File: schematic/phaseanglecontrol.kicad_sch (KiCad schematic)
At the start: 35 parts, among them J1 L_supply, J2 N_supply, J3 motor_housing, J4 N_motor, J5 L_motor, Q1 IRFP450, Q2 BS170, Q3 IRFR9310, Q4 IRFP450, U1 ATtiny861A-P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

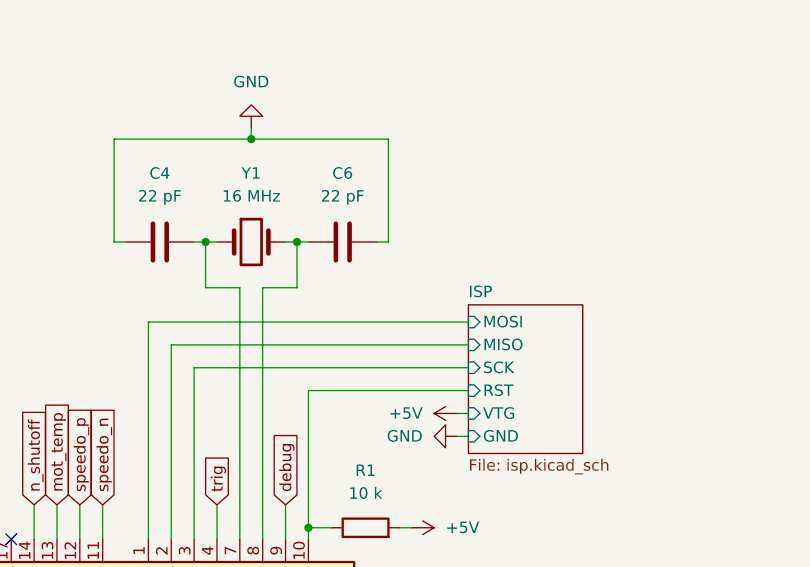
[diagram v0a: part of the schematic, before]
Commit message: schematic: Add uart tx
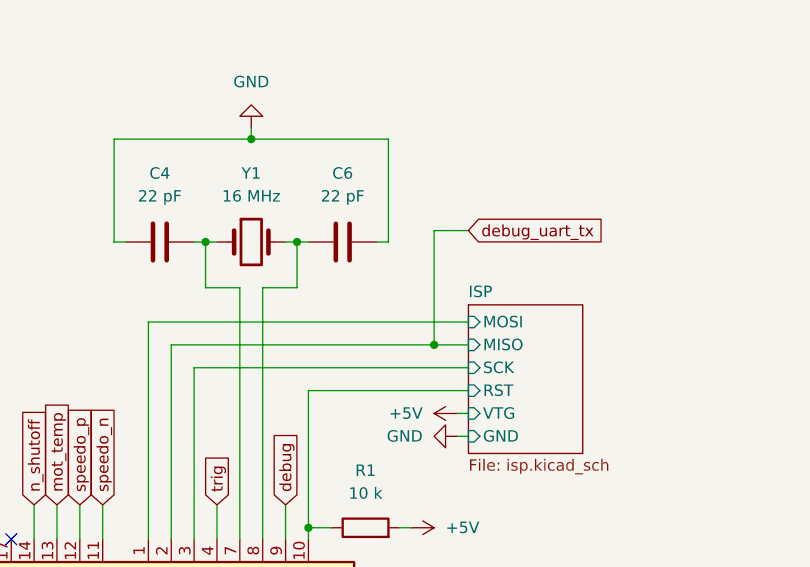
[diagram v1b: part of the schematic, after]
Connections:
- net ISP/MISO renamed debug_uart_tx
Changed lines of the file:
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@@
+	)
+	(junction
+		(at 105.41 128.27)
+		(diameter 0)
+		(color 0 0 0 0)
 	)
 	(junction
@@
 	(wire
 		(pts
-			(xy 76.2 128.27) (xy 109.22 128.27)
+			(xy 76.2 128.27) (xy 105.41 128.27)
 		)
 		(stroke
@@
 	(wire
 		(pts
+			(xy 105.41 115.57) (xy 105.41 128.27)
+		)
+		(stroke
+			(width 0)
+			(type default)
+		)
+	)
+	(wire
+		(pts
 			(xy 247.65 116.84) (xy 251.46 116.84)
 		)
@@
 	(wire
 		(pts
+			(xy 109.22 115.57) (xy 105.41 115.57)
+		)
+		(stroke
+			(width 0)
+			(type default)
+		)
+	)
+	(wire
+		(pts
 			(xy 172.72 111.76) (xy 168.91 111.76)
 		)
@@
 		(pts
 			(xy 137.16 27.94) (xy 147.32 27.94)
+		)
+		(stroke
+			(width 0)
+			(type default)
+		)
+	)
+	(wire
+		(pts
+			(xy 105.41 128.27) (xy 109.22 128.27)
 		)
 		(stroke
@@
 				(hide yes)
 			)
+		)
+	)
+	(global_label "debug_uart_tx"
+		(shape input)
+		(at 109.22 115.57 0)
+		(fields_autoplaced yes)
+		(effects
+			(font
+				(size 1.27 1.27)
+			)
+			(justify left)
+		)
+		(property "Intersheetrefs" "${INTERSHEET_REFS}"
+			(at 125.3887 115.57 0)
+			(effects
+				(font
+					(size 1.27 1.27)
+				)
+				(justify left)
+				(hide yes)
+			)

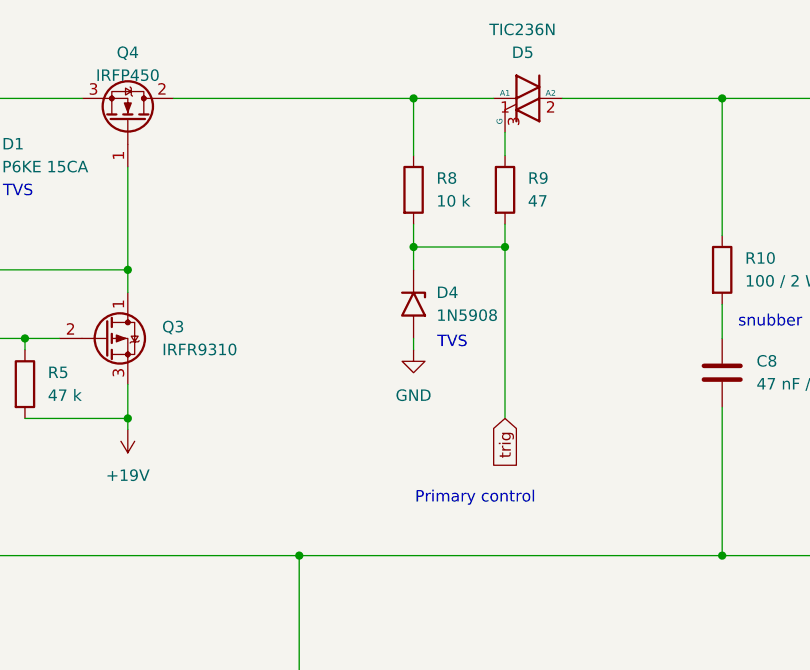
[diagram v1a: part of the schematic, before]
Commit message: schematic: Update trig resistor
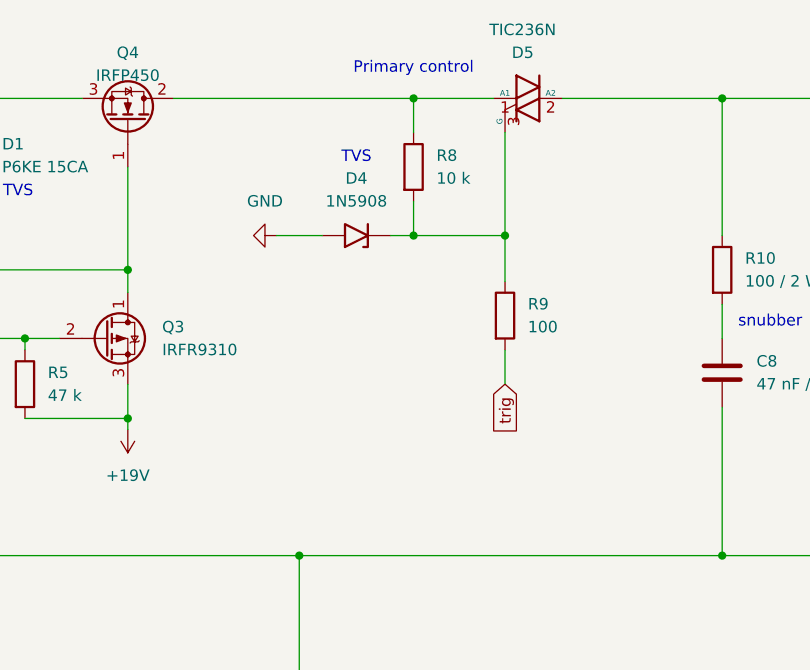
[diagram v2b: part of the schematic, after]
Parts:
- R9: value 47 -> 100
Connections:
- net trig: no longer D4.1 (A1), R8.2
- net at D5.3 (G), R9.1: now also D4.1 (A1), R8.2
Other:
- moved on the sheet: D4, R8, R9
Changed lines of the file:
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@@
 	(text "TVS"
 		(exclude_from_sim no)
-		(at 210.058 55.118 0)
+		(at 199.39 34.544 0)
 		(effects
 			(font
@@
 	(text "Primary control"
 		(exclude_from_sim no)
-		(at 212.598 72.39 0)
+		(at 205.74 24.638 0)
 		(effects
 			(font
@@
 	)
 	(junction
-		(at 60.96 27.94)
+		(at 205.74 43.18)
 		(diameter 0)
 		(color 0 0 0 0)
 	)
 	(junction
-		(at 137.16 27.94)
+		(at 60.96 27.94)
 		(diameter 0)
 		(color 0 0 0 0)
 	)
 	(junction
-		(at 147.32 27.94)
+		(at 137.16 27.94)
 		(diameter 0)
 		(color 0 0 0 0)
 	)
 	(junction
-		(at 157.48 46.99)
+		(at 147.32 27.94)
 		(diameter 0)
 		(color 0 0 0 0)
 	)
 	(junction
-		(at 205.74 44.45)
+		(at 157.48 46.99)
 		(diameter 0)
 		(color 0 0 0 0)
@@
 	)
 	(junction
-		(at 215.9 44.45)
+		(at 215.9 43.18)
 		(diameter 0)
 		(color 0 0 0 0)
@@
 	(wire
 		(pts
+			(xy 215.9 31.75) (xy 215.9 43.18)
+		)
+		(stroke
+			(width 0)
+			(type default)
+		)
+	)
+	(wire
+		(pts
 			(xy 193.04 78.74) (xy 240.03 78.74)
 		)
@@
 	(wire
 		(pts
-			(xy 215.9 31.75) (xy 215.9 34.29)
-		)
-		(stroke
-			(width 0)
-			(type default)
-		)
-	)
-	(wire
-		(pts
 			(xy 76.2 149.86) (xy 76.2 128.27)
 		)
@@
 	(wire
 		(pts
-			(xy 205.74 54.61) (xy 205.74 55.88)
-		)
-		(stroke
-			(width 0)
-			(type default)
-		)
-	)
-	(wire
-		(pts
 			(xy 222.25 27.94) (xy 240.03 27.94)
 		)
@@
 	(wire
 		(pts
-			(xy 205.74 41.91) (xy 205.74 44.45)
+			(xy 205.74 39.37) (xy 205.74 43.18)
 		)
 		(stroke
@@
 	(wire
 		(pts
+			(xy 190.5 43.18) (xy 195.58 43.18)
+		)
+		(stroke
+			(width 0)
+			(type default)
+		)
+	)
+	(wire
+		(pts
 			(xy 40.64 167.64) (xy 41.91 167.64)
 		)
@@
 	(wire
 		(pts
-			(xy 205.74 44.45) (xy 215.9 44.45)
+			(xy 205.74 43.18) (xy 215.9 43.18)
 		)
 		(stroke
@@
 	(wire
 		(pts
-			(xy 215.9 41.91) (xy 215.9 44.45)
-		)
-		(stroke
-			(width 0)
-			(type default)
-		)
-	)
-	(wire
-		(pts
 			(xy 137.16 46.99) (xy 147.32 46.99)
 		)
@@
 	(wire
 		(pts
-			(xy 205.74 44.45) (xy 205.74 46.99)
+			(xy 29.21 78.74) (xy 60.96 78.74)
 		)
 		(stroke
@@
 	(wire
 		(pts
-			(xy 29.21 78.74) (xy 60.96 78.74)
+			(xy 31.75 162.56) (xy 41.91 162.56)
 		)
 		(stroke
@@
 	(wire
 		(pts
-			(xy 31.75 162.56) (xy 41.91 162.56)
+			(xy 78.74 116.84) (xy 80.01 116.84)
 		)
 		(stroke
@@
 	(wire
 		(pts
-			(xy 78.74 116.84) (xy 80.01 116.84)
+			(xy 29.21 27.94) (xy 35.56 27.94)
 		)
 		(stroke
@@
 	(wire
 		(pts
-			(xy 29.21 27.94) (xy 35.56 27.94)
+			(xy 203.2 43.18) (xy 205.74 43.18)
 		)
 		(stroke
@@
 	(wire
 		(pts
-			(xy 205.74 27.94) (xy 205.74 34.29)
+			(xy 205.74 27.94) (xy 205.74 31.75)
 		)
 		(stroke
@@
 	(wire
 		(pts
-			(xy 215.9 44.45) (xy 215.9 63.5)
+			(xy 215.9 43.18) (xy 215.9 48.26)
 		)
 		(stroke
@@
 	(wire
 		(pts
+			(xy 215.9 55.88) (xy 215.9 59.69)
+		)
+		(stroke
+			(width 0)
+			(type default)
+		)
+	)
+	(wire
+		(pts
 			(xy 86.36 121.92) (xy 86.36 149.86)
 		)
@@
 	(global_label "trig"
 		(shape input)
-		(at 215.9 63.5 270)
+		(at 215.9 59.69 270)
 		(fields_autoplaced yes)
 		(effects
@@
 		)
 		(property "Intersheetrefs" "${INTERSHEET_REFS}"
-			(at 215.9 69.7509 90)
+			(at 215.9 65.9409 90)
 			(effects
 				(font
@@
 	(symbol
 		(lib_id "Diode:1N5908")
-		(at 205.74 50.8 270)
+		(at 199.39 43.18 180)
 		(unit 1)
 		(exclude_from_sim no)
@@
 		(fields_autoplaced yes)
 		(property "Reference" "D4"
-			(at 208.28 49.5299 90)
+			(at 199.39 36.83 0)
 			(effects
 				(font
 					(size 1.27 1.27)
 				)
-				(justify left)
 			)
 		)
 		(property "Value" "1N5908"
-			(at 208.28 52.0699 90)
+			(at 199.39 39.37 0)
 			(effects
 				(font
 					(size 1.27 1.27)
 				)
-				(justify left)
 			)
 		)
 		(property "Footprint" "Diode_THT:D_DO-201AE_P15.24mm_Horizontal"
-			(at 197.104 50.8 0)
+			(at 199.39 34.544 0)
 			(effects
 				(font
@@
 		)
 		(property "Datasheet" "https://www.st.com/resource/en/datasheet/1n5908.pdf"
-			(at 201.168 49.784 0)
+			(at 200.406 38.608 0)
 			(effects
 				(font
@@
 		)
 		(property "Description" "1500W (10/1000 μs) Unidirectional TVS Diode, VRM = 5V (IRM = 300 μA at 25°C), VBR = 6V, DO-201AE"
-			(at 199.136 50.8 0)
+			(at 199.39 36.576 0)
 			(effects
 				(font
@@
 	(symbol
 		(lib_id "Device:R")
-		(at 215.9 38.1 0)
+		(at 215.9 52.07 0)
 		(unit 1)
 		(exclude_from_sim no)
@@
 		(fields_autoplaced yes)
 		(property "Reference" "R9"
-			(at 218.44 36.8299 0)
+			(at 218.44 50.7999 0)
 			(effects
 				(font
@@
 			)
 		)
-		(property "Value" "47"
-			(at 218.44 39.3699 0)
+		(property "Value" "100"
+			(at 218.44 53.3399 0)
 			(effects
 				(font
@@
 		)
 		(property "Footprint" ""
-			(at 214.122 38.1 90)
+			(at 214.122 52.07 90)
 			(effects
 				(font
@@
 		)
 		(property "Datasheet" "~"
-			(at 215.9 38.1 0)
+			(at 215.9 52.07 0)
 			(effects
 				(font
@@
 		)
 		(property "Description" "Resistor"
-			(at 215.9 38.1 0)
+			(at 215.9 52.07 0)
 			(effects
 				(font
@@
 	(symbol
 		(lib_id "Device:R")
-		(at 205.74 38.1 0)
+		(at 205.74 35.56 0)
 		(unit 1)
 		(exclude_from_sim no)
@@
 		(fields_autoplaced yes)
 		(property "Reference" "R8"
-			(at 208.28 36.8299 0)
+			(at 208.28 34.2899 0)
 			(effects
 				(font
@@
 		)
 		(property "Value" "10 k"
-			(at 208.28 39.3699 0)
+			(at 208.28 36.8299 0)
 			(effects
 				(font
@@
 		)
 		(property "Footprint" ""
-			(at 203.962 38.1 90)
+			(at 203.962 35.56 90)
 			(effects
 				(font
@@
 		)
 		(property "Datasheet" "~"
-			(at 205.74 38.1 0)
+			(at 205.74 35.56 0)
 			(effects
 				(font
@@
 		)
 		(property "Description" "Resistor"
-			(at 205.74 38.1 0)
+			(at 205.74 35.56 0)
 			(effects
 				(font
@@
 	(symbol
 		(lib_id "power:GND")
-		(at 205.74 55.88 0)
+		(at 190.5 43.18 270)
 		(unit 1)
 		(exclude_from_sim no)
@@
 		(fields_autoplaced yes)
 		(property "Reference" "#PWR014"
-			(at 205.74 62.23 0)
+			(at 184.15 43.18 0)
 			(effects
 				(font
@@
 		)
 		(property "Value" "GND"
-			(at 205.74 60.96 0)
+			(at 189.23 39.37 90)
 			(effects
 				(font
@@
 		)
 		(property "Footprint" ""
-			(at 205.74 55.88 0)
+			(at 190.5 43.18 0)
 			(effects
 				(font
@@
 		)
 		(property "Datasheet" ""
-			(at 205.74 55.88 0)
+			(at 190.5 43.18 0)
 			(effects
 				(font
@@
 		)
 		(property "Description" "Power symbol creates a global label with name \"GND\" , ground"
-			(at 205.74 55.88 0)
+			(at 190.5 43.18 0)
 			(effects
 				(font

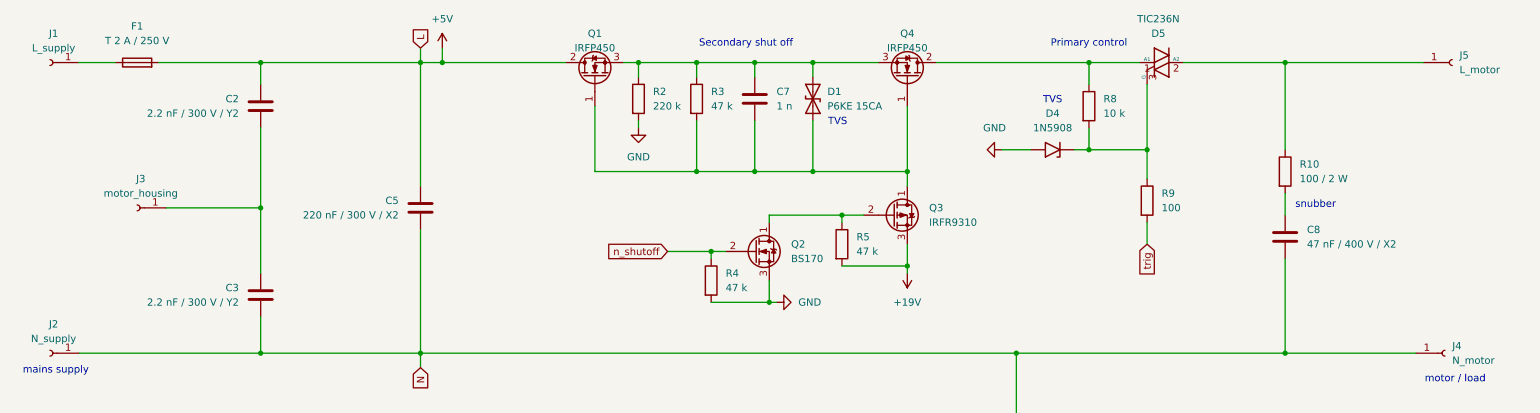
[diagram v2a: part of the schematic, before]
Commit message: schematic: Minor cleanups
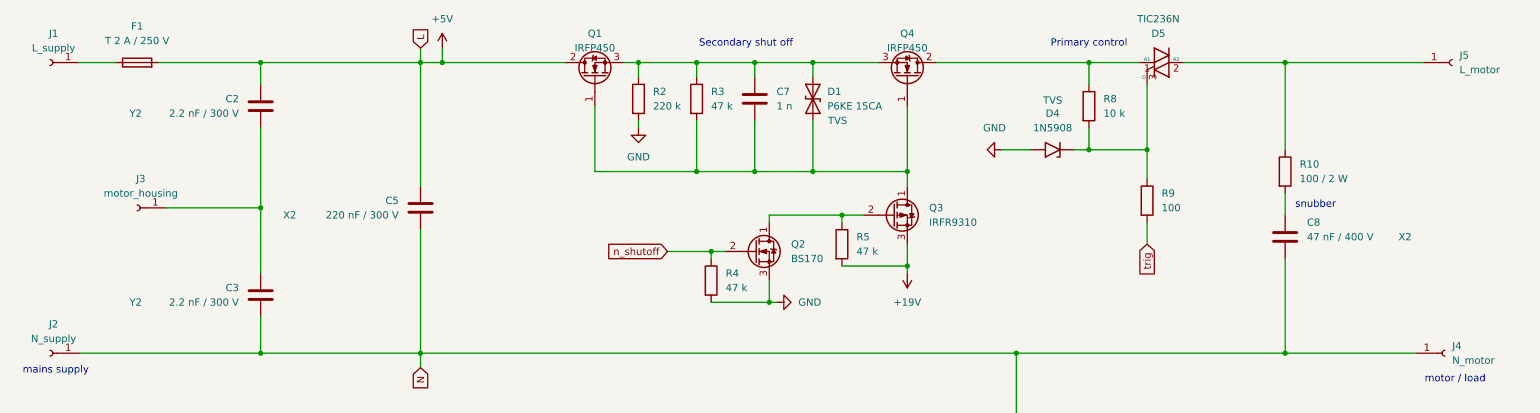
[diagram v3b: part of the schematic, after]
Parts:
- C2, C3: value 2.2 nF / 300 V / Y2 -> 2.2 nF / 300 V
- C5: value 220 nF / 300 V / X2 -> 220 nF / 300 V
- C8: value 47 nF / 400 V / X2 -> 47 nF / 400 V
- Q1, Q4: footprint Package_TO_SOT_THT:TO-247-3_Vertical -> (none)
- Q3: footprint Package_TO_SOT_THT:TO-92_Inline -> (none)
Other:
- note removed: "TVS"
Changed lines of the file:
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@@
 		(company "Michael Büsch <m@bues.ch>")
 	)
-	(text "TVS"
-		(exclude_from_sim no)
-		(at 199.39 34.544 0)
-		(effects
-			(font
-				(size 1.27 1.27)
-			)
-		)
-	)
 	(text "snubber"
 		(exclude_from_sim no)
@@
 		)
 	)
-	(text "TVS"
-		(exclude_from_sim no)
-		(at 161.798 38.354 0)
-		(effects
-			(font
-				(size 1.27 1.27)
-			)
-		)
-	)
 	(text "Primary control"
 		(exclude_from_sim no)
@@
 			)
 		)
-		(property "Value" "2.2 nF / 300 V / Y2"
+		(property "Value" "2.2 nF / 300 V"
 			(at 57.15 36.8299 0)
 			(effects
@@
 			)
 		)
-		(property "Description" "Unpolarized capacitor"
-			(at 60.96 35.56 0)
+		(property "Description" "Y2"
+			(at 39.116 36.83 0)
 			(effects
 				(font
 					(size 1.27 1.27)
 				)
-				(hide yes)
 			)
 		)
@@
 			)
 		)
-		(property "Footprint" "Package_TO_SOT_THT:TO-247-3_Vertical"
+		(property "Footprint" ""
 			(at 121.285 25.4 0)
 			(effects
@@
 			)
 		)
-		(property "Datasheet" "https://www.infineon.com/dgdl/irfp4468pbf.pdf?fileId=5546d462533600a40153562c73472019"
+		(property "Datasheet" ""
 			(at 123.19 25.4 0)
 			(effects
@@
 			)
 		)
-		(property "Description" "195A Id, 100V Vds, N-Channel Power MOSFET, TO-247"
+		(property "Description" ""
 			(at 119.38 30.48 0)
 			(effects
@@
 		(on_board yes)
 		(dnp no)
-		(fields_autoplaced yes)
 		(property "Reference" "D4"
 			(at 199.39 36.83 0)
@@
 			)
 		)
-		(property "Description" "1500W (10/1000 μs) Unidirectional TVS Diode, VRM = 5V (IRM = 300 μA at 25°C), VBR = 6V, DO-201AE"
-			(at 199.39 36.576 0)
+		(property "Description" "TVS"
+			(at 199.39 34.544 0)
 			(effects
 				(font
 					(size 1.27 1.27)
 				)
-				(hide yes)
 			)
 		)
@@
 			)
 		)
-		(property "Value" "2.2 nF / 300 V / Y2"
+		(property "Value" "2.2 nF / 300 V"
 			(at 57.15 69.8499 0)
 			(effects
@@
 			)
 		)
-		(property "Description" "Unpolarized capacitor"
-			(at 60.96 68.58 0)
+		(property "Description" "Y2"
+			(at 39.116 69.85 0)
 			(effects
 				(font
 					(size 1.27 1.27)
 				)
-				(hide yes)
 			)
 		)
@@
 		(on_board yes)
 		(dnp no)
-		(fields_autoplaced yes)
 		(property "Reference" "C8"
-			(at 243.84 57.1499 0)
+			(at 243.84 55.8799 0)
 			(effects
 				(font
@@
 			)
 		)
-		(property "Value" "47 nF / 400 V / X2"
-			(at 243.84 59.6899 0)
+		(property "Value" "47 nF / 400 V"
+			(at 243.84 58.4199 0)
 			(effects
 				(font
@@
 			)
 		)
-		(property "Description" "Unpolarized capacitor"
-			(at 240.03 58.42 0)
+		(property "Description" "X2"
+			(at 259.842 58.42 0)
 			(effects
 				(font
 					(size 1.27 1.27)
 				)
-				(hide yes)
+				(justify left)
 			)
 		)
@@
 			)
 		)
-		(property "Value" "220 nF / 300 V / X2"
+		(property "Value" "220 nF / 300 V"
 			(at 85.09 54.6099 0)
 			(effects
@@
 			)
 		)
-		(property "Datasheet" "~"
+		(property "Datasheet" ""
 			(at 88.9 53.34 0)
 			(effects
@@
 			)
 		)
-		(property "Description" "Unpolarized capacitor"
-			(at 88.9 53.34 0)
+		(property "Description" "X2"
+			(at 66.04 54.61 0)
 			(effects
 				(font
 					(size 1.27 1.27)
 				)
-				(hide yes)
 			)
 		)
@@
 			)
 		)
-		(property "Footprint" "Package_TO_SOT_THT:TO-247-3_Vertical"
+		(property "Footprint" ""
 			(at 172.085 25.4 0)
 			(effects
@@
 			)
 		)
-		(property "Datasheet" "https://www.infineon.com/dgdl/irfp4468pbf.pdf?fileId=5546d462533600a40153562c73472019"
+		(property "Datasheet" ""
 			(at 170.18 25.4 0)
 			(effects
@@
 			)
 		)
-		(property "Description" "195A Id, 100V Vds, N-Channel Power MOSFET, TO-247"
+		(property "Description" ""
 			(at 173.99 30.48 0)
 			(effects
@@
 			)
 		)
-		(property "Footprint" "Package_TO_SOT_THT:TO-92_Inline"
+		(property "Footprint" ""
 			(at 176.53 56.515 0)
 			(effects
@@
 			)
 		)
-		(property "Datasheet" "http://www.vishay.com/docs/70209/70209.pdf"
+		(property "Datasheet" ""
 			(at 176.53 58.42 0)
 			(effects
@@
 			)
 		)
-		(property "Description" "-0.18A Id, -45V Vds, P-Channel MOSFET, TO-92"
+		(property "Description" ""
 			(at 171.45 54.61 0)
 			(effects
@@
 		(on_board yes)
 		(dnp no)
-		(fields_autoplaced yes)
 		(property "Reference" "D1"
 			(at 160.02 33.0199 90)
@@
 			)
 		)
-		(property "Description" "1500W bidirectional TRANSZORB® Transient Voltage Suppressor, DO-201AE"
-			(at 157.48 34.29 0)
+		(property "Description" "TVS"
+			(at 161.798 38.1 90)
 			(effects
 				(font
 					(size 1.27 1.27)
 				)
-				(hide yes)
 			)
 		)
